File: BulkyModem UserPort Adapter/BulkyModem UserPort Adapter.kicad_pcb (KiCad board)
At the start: 2 copper layers, 70.7 x 30 mm, 9 parts, among them J1 C64_UserPort, J3 C64_Modem_IDC, M1 Mounting, M2 Mounting, M3 Mounting, M4 Mounting

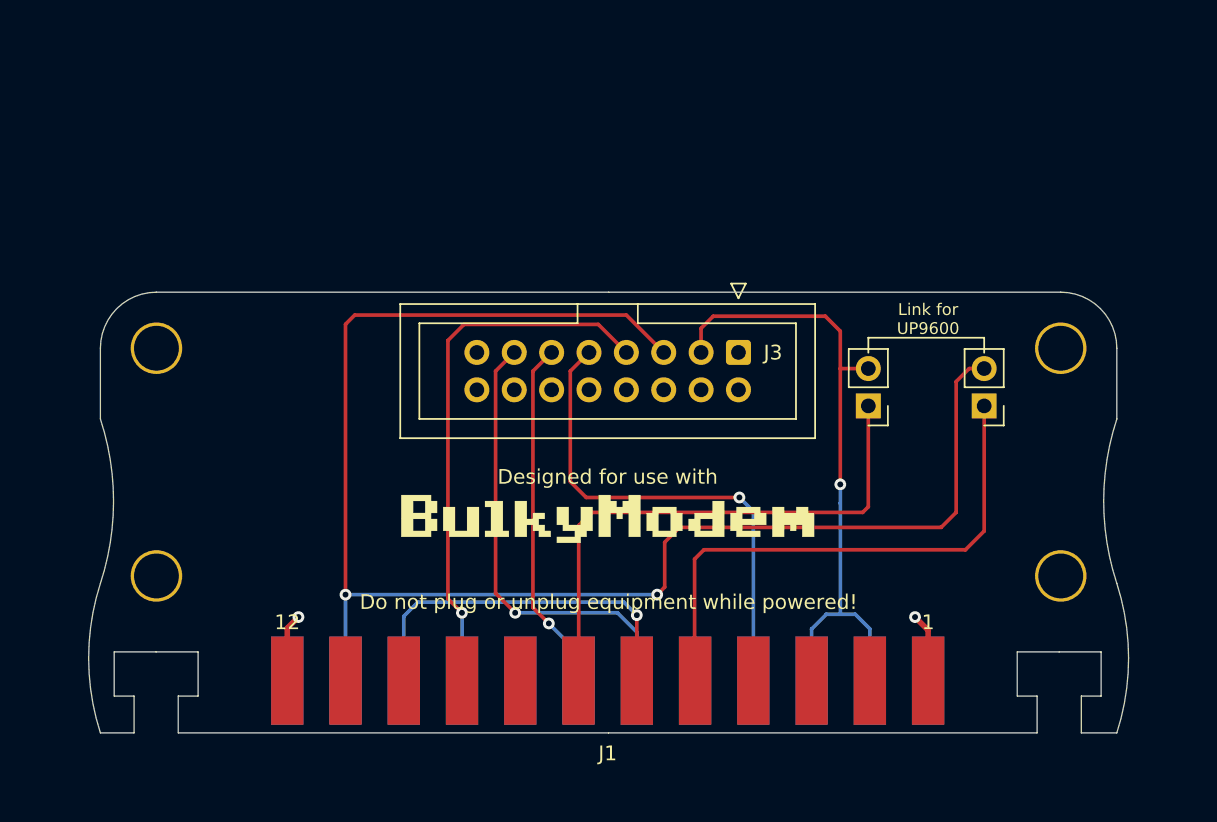
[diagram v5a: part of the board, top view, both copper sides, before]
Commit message: New UserPort Adapter
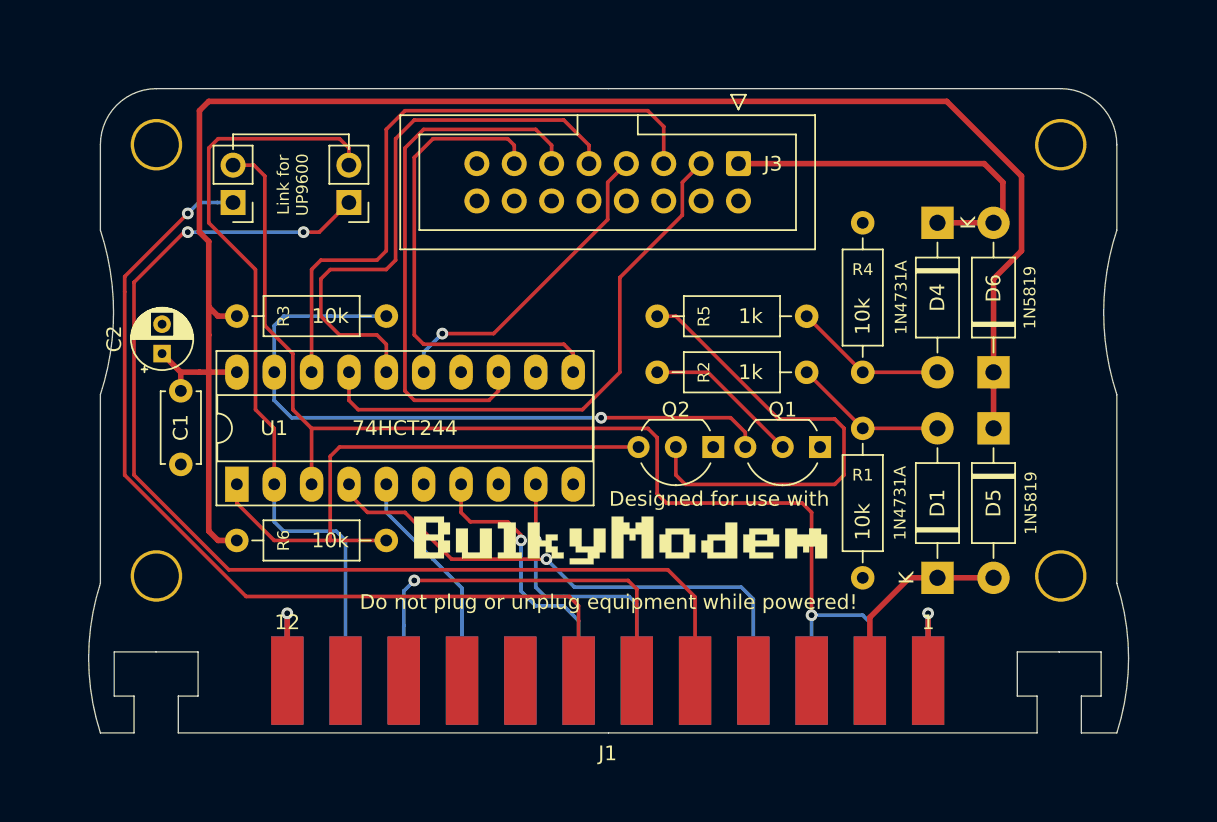
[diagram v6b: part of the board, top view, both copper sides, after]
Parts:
- added C1: 100nF, Capacitor_THT:C_Disc_D4.7mm_W2.5mm_P5.00mm, F.Cu at (122.6, 85.7)
- added C2: 10uF, Capacitor_THT:CP_Radial_D4.0mm_P2.00mm, F.Cu at (121.3, 83.2)
- added D1: 1N4731A, Diode_THT:D_DO-41_SOD81_P10.16mm_Horizontal, F.Cu at (174.0, 98.4)
- added D4: 1N4731A, Diode_THT:D_DO-41_SOD81_P10.16mm_Horizontal, F.Cu at (174.0, 74.3)
- added D5: 1N5819, BulkyModem:D_DO-41_SOD81_P10.16mm_Horizontal, F.Cu at (177.8, 88.3)
- added D6: 1N5819, BulkyModem:D_DO-41_SOD81_P10.16mm_Horizontal, F.Cu at (177.8, 84.5)
- added Q1: 2N3904, Package_TO_SOT_THT:TO-92_Inline_Wide, F.Cu at (166.0, 89.5)
- added Q2: 2N3904, Package_TO_SOT_THT:TO-92_Inline_Wide, F.Cu at (158.8, 89.5)
- added R1: 10k, resistor:R_Axial_DIN0207_L6.3mm_D2.5mm_P10.16mm_Horizontal, F.Cu at (168.9, 88.3)
- added R2: 1k, resistor:R_Axial_DIN0207_L6.3mm_D2.5mm_P10.16mm_Horizontal, F.Cu at (154.9, 84.5)
- added R3: 10k, resistor:R_Axial_DIN0207_L6.3mm_D2.5mm_P10.16mm_Horizontal, F.Cu at (126.4, 80.6)
- added R4: 10k, resistor:R_Axial_DIN0207_L6.3mm_D2.5mm_P10.16mm_Horizontal, F.Cu at (168.9, 84.5)
- added R5: 1k, resistor:R_Axial_DIN0207_L6.3mm_D2.5mm_P10.16mm_Horizontal, F.Cu at (154.9, 80.6)
- added R6: 10k, resistor:R_Axial_DIN0207_L6.3mm_D2.5mm_P10.16mm_Horizontal, F.Cu at (126.4, 95.9)
- added U1: 74HCT244, Package_DIP:DIP-20_W7.62mm_Socket_LongPads, F.Cu at (126.4, 92.1)
- J3: value C64_Modem_IDC -> BulkyModem
- moved JP2 45.3 mm to (126.1, 72.9)
- moved JP1 45.3 mm to (134.0, 72.9)
- moved M3 13.8 mm to (182.4, 69.0)
- moved M4 13.8 mm to (120.9, 69.0)
- moved J3 12.8 mm to (160.5, 70.3)
- moved G*** 1.70 mm to (152.5, 95.9)
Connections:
- J1 pad 10: (no net) -> unconnected-(J1-9VAC-Pad10)
- J1 pad 11: (no net) -> unconnected-(J1-9VAC-Pad11)
- J1 pad 2: (no net) -> VCC_C64
- J1 pad 3: (no net) -> unconnected-(J1-~{RESET}-Pad3)
- J1 pad 4: (no net) -> unconnected-(J1-CNT1-Pad4)
- J1 pad 8: (no net) -> unconnected-(J1-~{PC2}-Pad8)
- J1 pad 9: (no net) -> unconnected-(J1-ATN-Pad9)
- J1 pad B: TXD -> C64_TXD
- J1 pad C: TXD -> C64_TXD
- J1 pad D: CTS -> C64_CTS
- J1 pad E: (no net) -> unconnected-(J1-PB2(DTR)-PadE)
- J1 pad F: RI -> C64_RI
- J1 pad H: DCD -> C64_DCD
- J1 pad J: (no net) -> unconnected-(J1-PB5-PadJ)
- J1 pad K: RTS -> C64_RTS
- J1 pad M: RXD -> C64_RXD
- J3 pad 1: (no net) -> VCC_MODEM
- J3 pad 16: (no net) -> unconnected-(J3-N.C.-Pad16)
- J3 pad 2: TXD -> MODEM_TXD
- J3 pad 3: RXD -> MODEM_RXD
- J3 pad 4: RTS -> MODEM_RTS
- J3 pad 5: CTS -> MODEM_CTS
- J3 pad 6: DCD -> MODEM_DCD
- J3 pad 7: RI -> MODEM_RI
- J3 pad 8: (no net) -> unconnected-(J3-N.C-Pad8)
- J3 pad 9: GND -> unconnected-(J3-N.C.-Pad9)
- JP1 pad 2: RXD -> C64_RXD
- JP2 pad 2: TXD -> C64_TXD
- M1 pad 1: (no net) -> GND
- M2 pad 1: (no net) -> GND
- M3 pad 1: (no net) -> GND
- M4 pad 1: (no net) -> GND
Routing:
- net VCC_ADAPTER: track 0.00 -> 116.2 mm
- net RXD: track 103.9 -> 0.00 mm, vias 2 -> 0
- net C64_TXD: track 0.00 -> 82.9 mm, vias 0 -> 1
- net C64_RXD: track 0.00 -> 53.4 mm
- net ~{C64_UP}: track 0.00 -> 46.9 mm, vias 0 -> 1
- net TXD: track 44.8 -> 0.00 mm, vias 1 -> 0
- net MODEM_RXD: track 0.00 -> 43.2 mm
- net Net-(J1-SP1): track 37.3 -> 77.2 mm, vias 0 -> 2
- net ~{MODEM_UP}: track 0.00 -> 39.4 mm
- net MODEM_CTS: track 0.00 -> 39.2 mm
- net MODEM_TXD: track 0.00 -> 38.1 mm
- net RTS: track 36.9 -> 0.00 mm, vias 1 -> 0
- net MODEM_DCD: track 0.00 -> 36.9 mm
- net C64_CTS: track 0.00 -> 36.6 mm, vias 0 -> 1
- net CTS: track 34.1 -> 0.00 mm, vias 1 -> 0
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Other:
- board size 70.7 x 30 mm -> 70.7 x 43.8 mm
- net class Default removed
- net class PWR removed

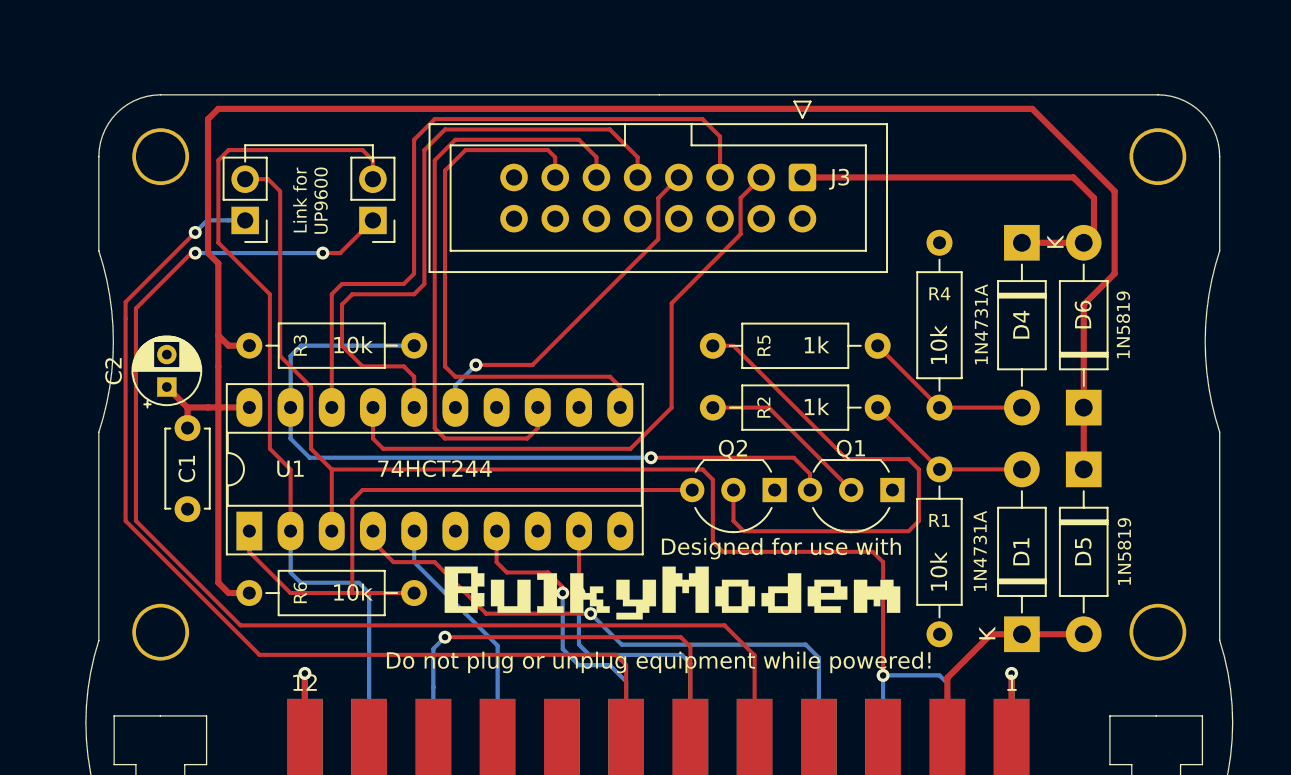
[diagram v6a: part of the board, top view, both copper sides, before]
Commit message: Change UserPort transmitter to only enable on both parties present
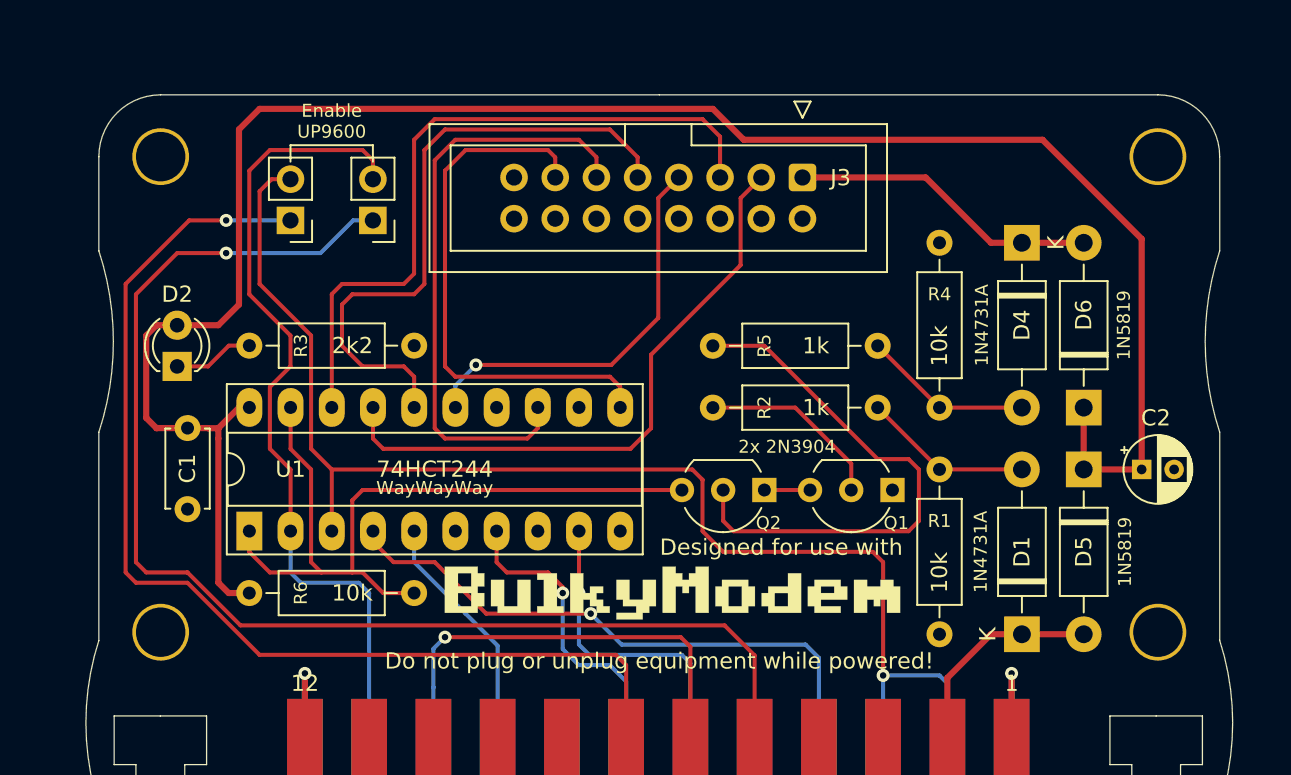
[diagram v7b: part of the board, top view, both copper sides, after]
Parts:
- added D2: PWR, LED_THT:LED_D3.0mm, F.Cu at (121.9, 81.9)
- R3: value 10k -> 2k2
- moved C2 60.3 mm to (181.4, 88.3), turned to 0 degrees
- moved JP2 2.79 mm to (128.9, 72.9)
- moved Q2 0.63 mm to (158.1, 89.5)
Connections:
- Q1 pad 3: ~{C64_UP} -> Net-(Q1-C)
- Q2 pad 1: GND -> Net-(Q1-C)
- Q2 pad 3: ~{MODEM_UP} -> ~{ADAPTER_EN}
- R3 pad 1: VCC_ADAPTER -> Net-(D2-K)
- R3 pad 2: ~{C64_UP} -> GND
- R6 pad 2: ~{MODEM_UP} -> ~{ADAPTER_EN}
- U1 pad 1: ~{MODEM_UP} -> ~{ADAPTER_EN}
- U1 pad 19: ~{C64_UP} -> ~{ADAPTER_EN}
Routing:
- net ~{ADAPTER_EN}: track 0.00 -> 47.8 mm
- net ~{C64_UP}: track 46.9 -> 0.00 mm, vias 1 -> 0
- net ~{MODEM_UP}: track 39.4 -> 0.00 mm
- net VCC_MODEM: track 25.4 -> 19.0 mm
- net VCC_ADAPTER: track 116.2 -> 122.3 mm
- net Net-(J1-SP2): track 62.6 -> 67.9 mm
- net Net-(D2-K): track 0.00 -> 4.98 mm
- net MODEM_RTS: track 22.1 -> 24.9 mm
- net Net-(Q1-C): track 0.00 -> 2.81 mm
- net C64_RXD: track 53.4 -> 51.3 mm
- net Net-(J1-SP1): track 77.2 -> 79.2 mm, vias 2 -> 1
- net Net-(Q1-B): track 10.6 -> 11.6 mm
- net Net-(Q2-B): track 32.9 -> 33.5 mm
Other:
- board text added: "2x 2N3904"
- board text added: "C64 BulkyModem UserPort Adapter (rev. C) github.com/tebl"
- board text added: "Enable UP9600"
- board text added: "WayWayWay"
- board text removed: "C64 BulkyModem UserPort Adapter github.com/tebl"
- board text removed: "Link for UP9600"

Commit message: Exported files
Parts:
- added D3: EN, LED_THT:LED_D3.0mm, F.Cu at (175.3, 70.3)
- added R7: 2k2, resistor:R_Axial_DIN0207_L6.3mm_D2.5mm_P10.16mm_Horizontal, F.Cu at (165.1, 78.1)
- moved D2 49.6 mm to (170.2, 70.3)
- moved R3 24.9 mm to (151.1, 78.1), turned to 180 degrees
- moved R5 0.64 mm to (154.9, 81.3)
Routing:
- net Net-(D2-K): track 4.98 -> 44.7 mm
- net Net-(D3-K): track 0.00 -> 25.8 mm
- net ~{ADAPTER_EN}: track 47.8 -> 60.1 mm, vias 0 -> 1
- net MODEM_CTS: track 39.2 -> 31.8 mm
- net VCC_ADAPTER: track 122.3 -> 116.8 mm
- net MODEM_TXD: track 38.1 -> 42.6 mm
- net VCC_MODEM: track 19.0 -> 22.1 mm
- net MODEM_RTS: track 24.9 -> 26.6 mm
- net C64_RXD: track 51.3 -> 50.3 mm
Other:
- board text added: "BulkyModem UserPort Adapter (rev. C) github.com/tebl"
- board text removed: "C64 BulkyModem UserPort Adapter (rev. C) github.com/tebl"
